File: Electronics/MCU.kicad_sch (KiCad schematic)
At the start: 6 parts

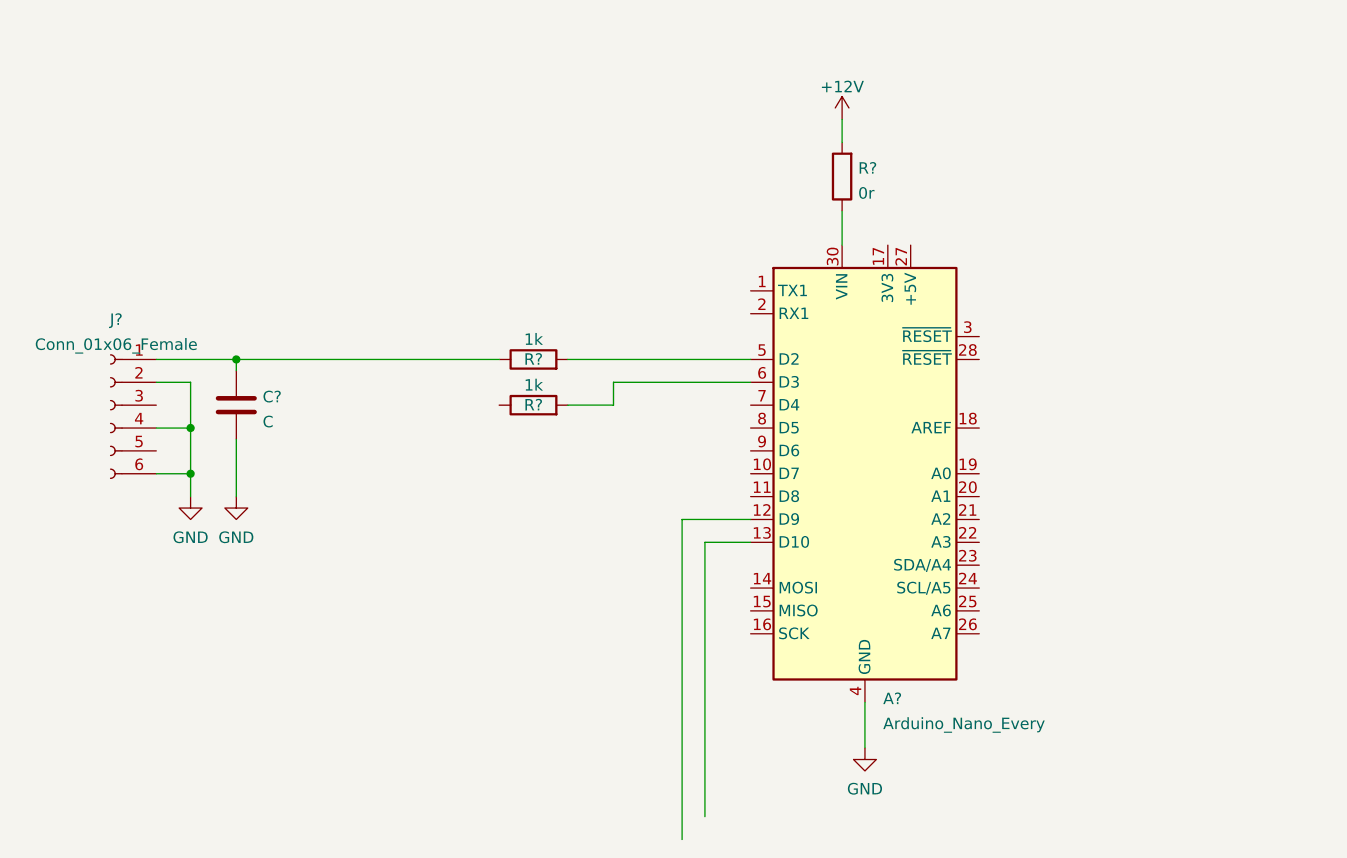
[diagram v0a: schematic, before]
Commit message: Added third half bridge for BLDC applications
Signed-off-by: Finder <aki.kuusela@findersee.fi>
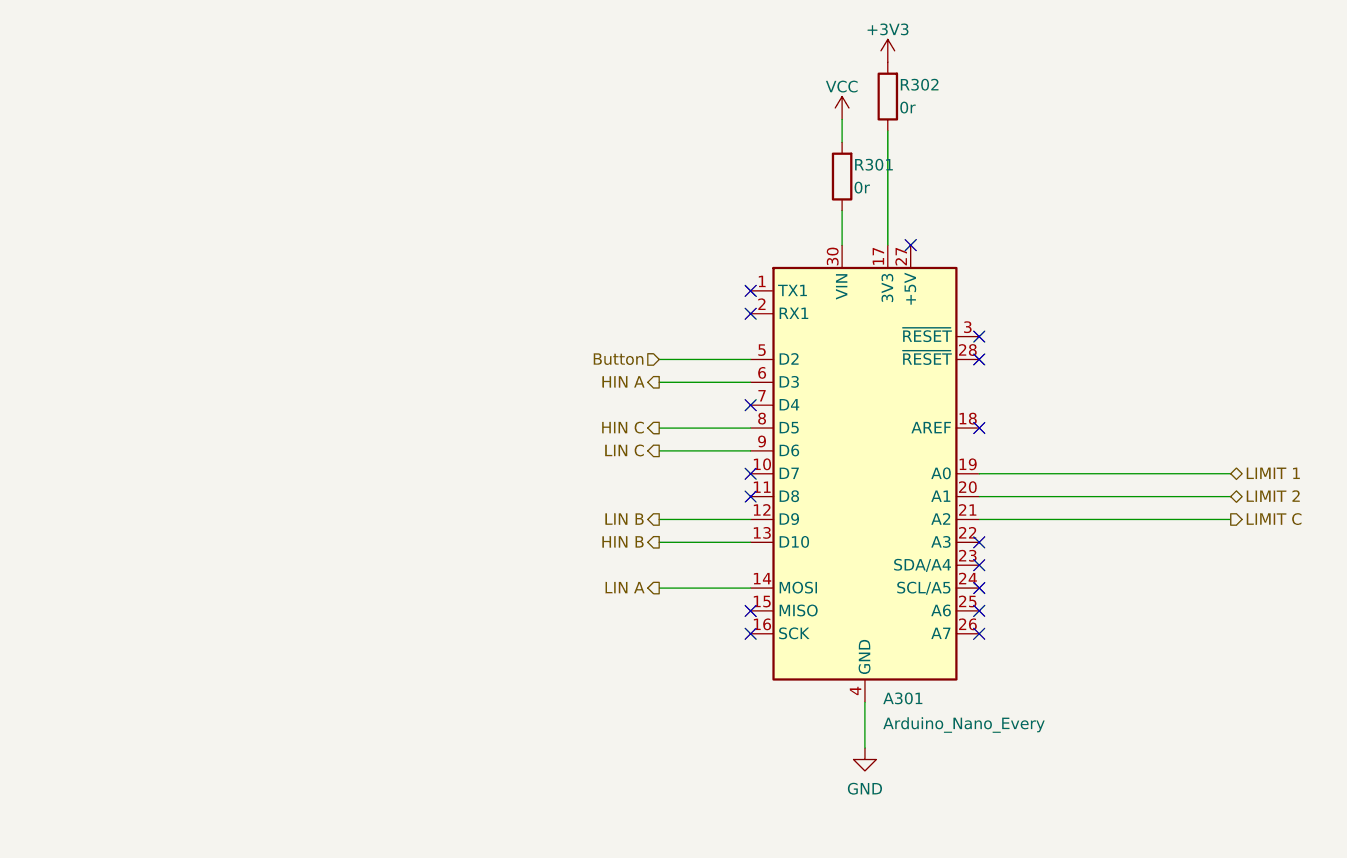
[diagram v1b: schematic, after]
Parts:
- removed C?: C, symbol Device:C
- removed J?: Conn_01x06_Female, TerminalBlock:TerminalBlock_bornier-6_P5.08mm, symbol Connector:Conn_01x06_Female
- removed R? (x2): 1k, digikey-footprints:0603, symbol Device:R
- added R302: 0r, digikey-footprints:0805, symbol Device:R
- gave numbers to parts that had none: 2
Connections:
- net HIN A: now reaches A301.6 (D3)
- net Button: now reaches A301.5 (D2)
- net LIN B: now reaches A301.12 (D9)
- net HIN B: now reaches A301.13 (D10)
- net LIN A: now reaches A301.14 (MOSI)
- net at A301.17 (3V3): now also R302.1
- net LIMIT 1: now reaches A301.19 (A0)
- net LIMIT 2: now reaches A301.20 (A1)
- net LIMIT C: now reaches A301.21 (A2)
- net HIN C: now reaches A301.8 (D5)
- net LIN C: now reaches A301.9 (D6)
- net +12V renamed VCC
- new net +3V3: R302.2
- no-connect marks 0 -> 16

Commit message: Layout update
Signed-off-by: Aki Kuusela <git@findersee.fi>
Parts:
- added C301: 100n, Capacitor_SMD:C_0603_1608Metric_Pad1.08x0.95mm_HandSolder, symbol Device:C
- added U301: 74HC86, Package_SO:SO-14_3.9x8.65mm_P1.27mm, symbol 74xx:74HC86
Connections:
- net +3V3: now also C301.2, U301.14 (VCC)
- net Button: now also U301.6
- net GND: now also C301.1, U301.10, U301.12, U301.13, U301.7 (GND), U301.9
- new net: U301.3, U301.4
- new net HALL A: U301.1
- new net HALL B: U301.2
- new net HALL C: U301.5
- no-connect marks 16 -> 18

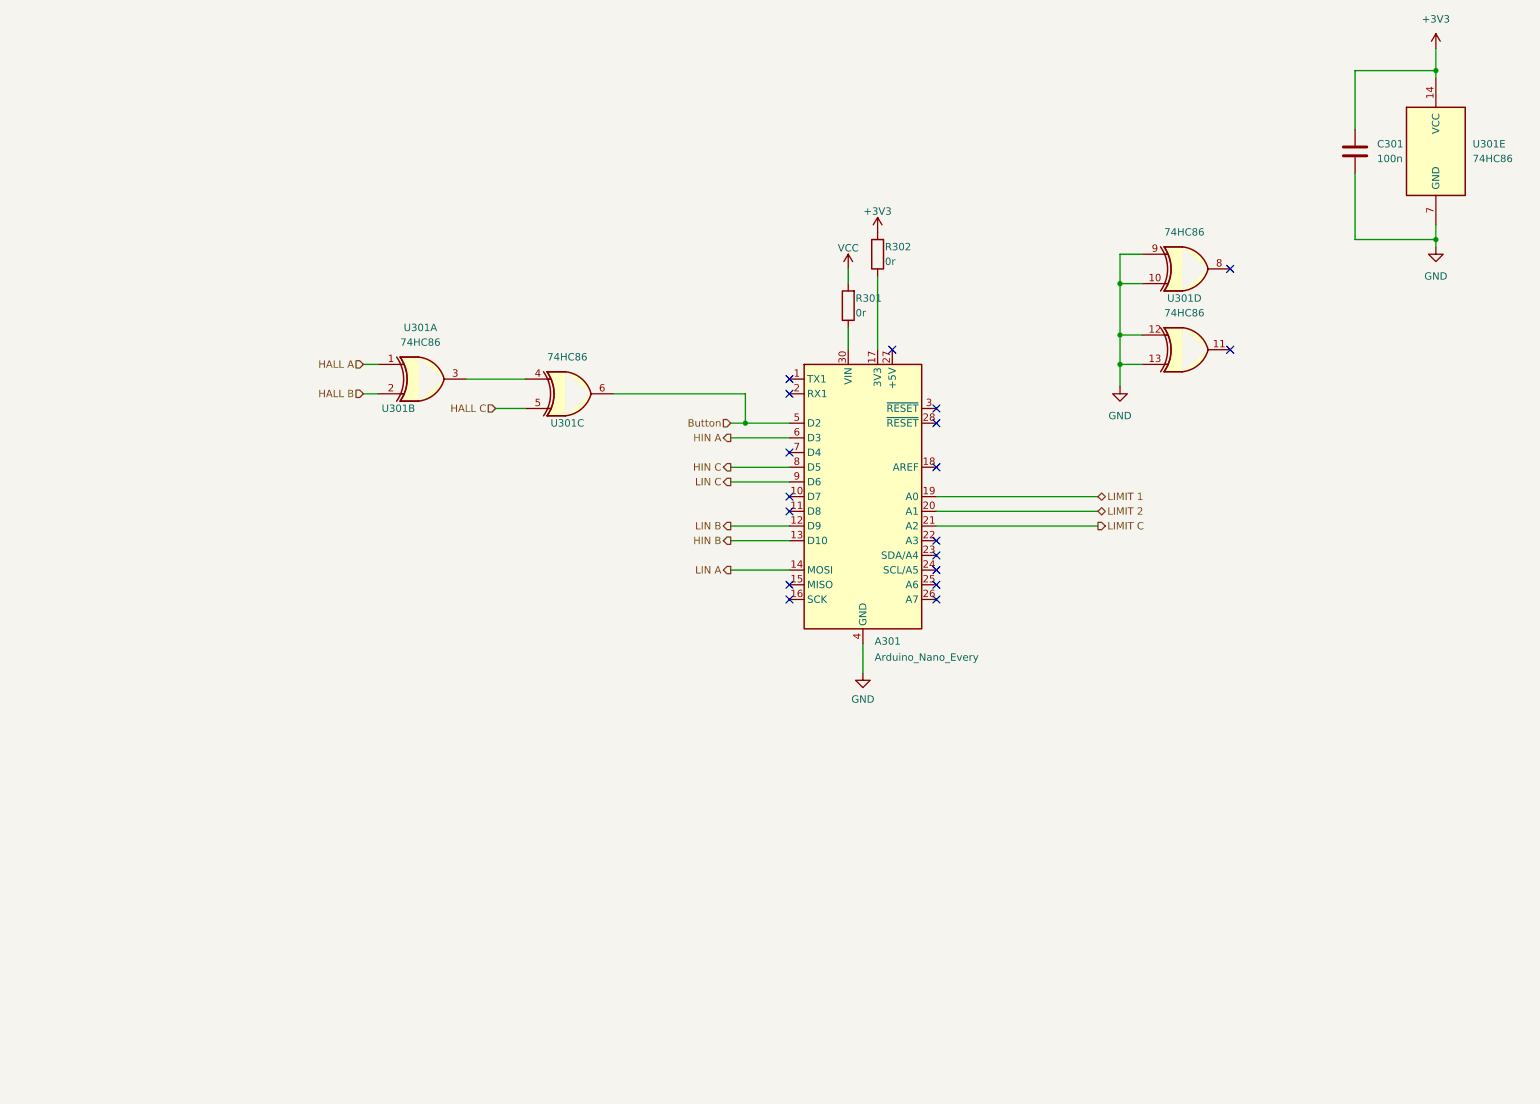
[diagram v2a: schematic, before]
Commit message: Added hall sensor circuitry
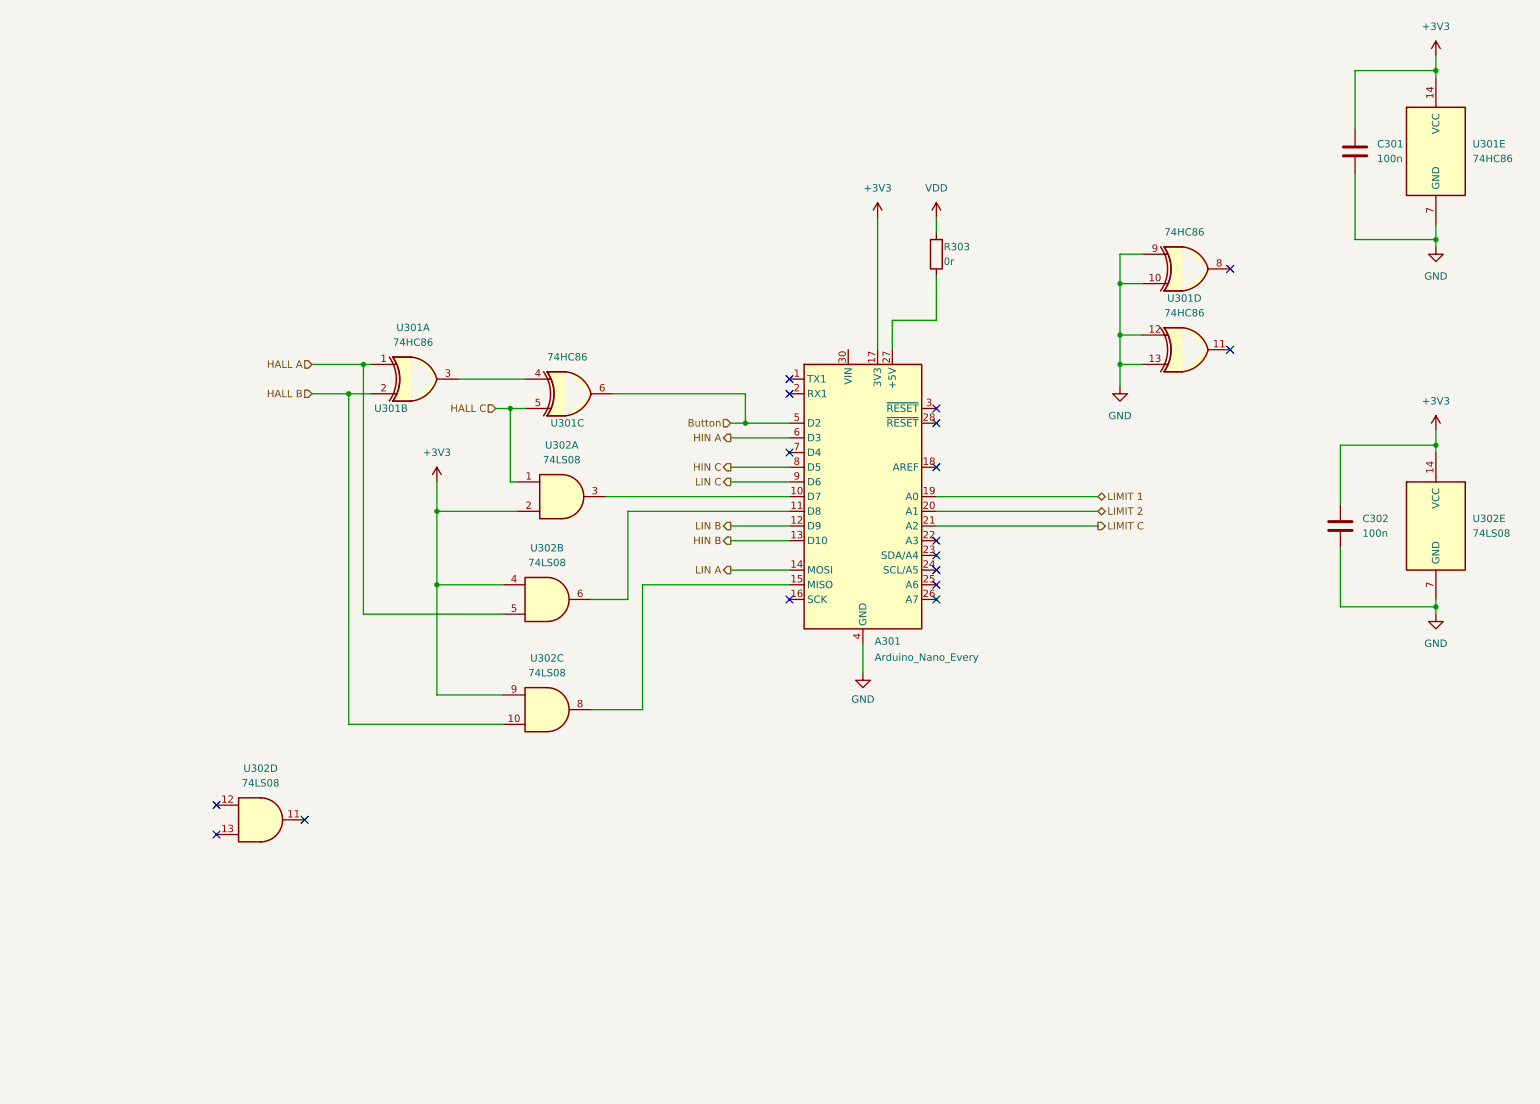
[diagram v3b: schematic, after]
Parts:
- removed R301, R302: 0r, digikey-footprints:0805, symbol Device:R
- added C302: 100n, Capacitor_SMD:C_0603_1608Metric_Pad1.08x0.95mm_HandSolder, symbol Device:C
- added R303: 0r, digikey-footprints:0805, symbol Device:R
- added U302: 74LS08, symbol 74xx:74LS08
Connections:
- net +3V3: now also A301.17 (3V3), C302.2, U302.14 (VCC), U302.2, U302.4, U302.9
- net GND: now also C302.1, U302.7 (GND)
- net HALL A: now also U302.5
- net HALL B: now also U302.10
- net HALL C: now also U302.1
- net at A301.10 (D7): now also U302.3
- net at A301.11 (D8): now also U302.6
- net at A301.15 (MISO): now also U302.8
- net at A301.27 (+5V): now also R303.1
- new net VDD: R303.2
- no-connect marks 18 -> 17
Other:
- moved on the sheet: U301A

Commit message: Added Current sensor finalized layout version 0.1
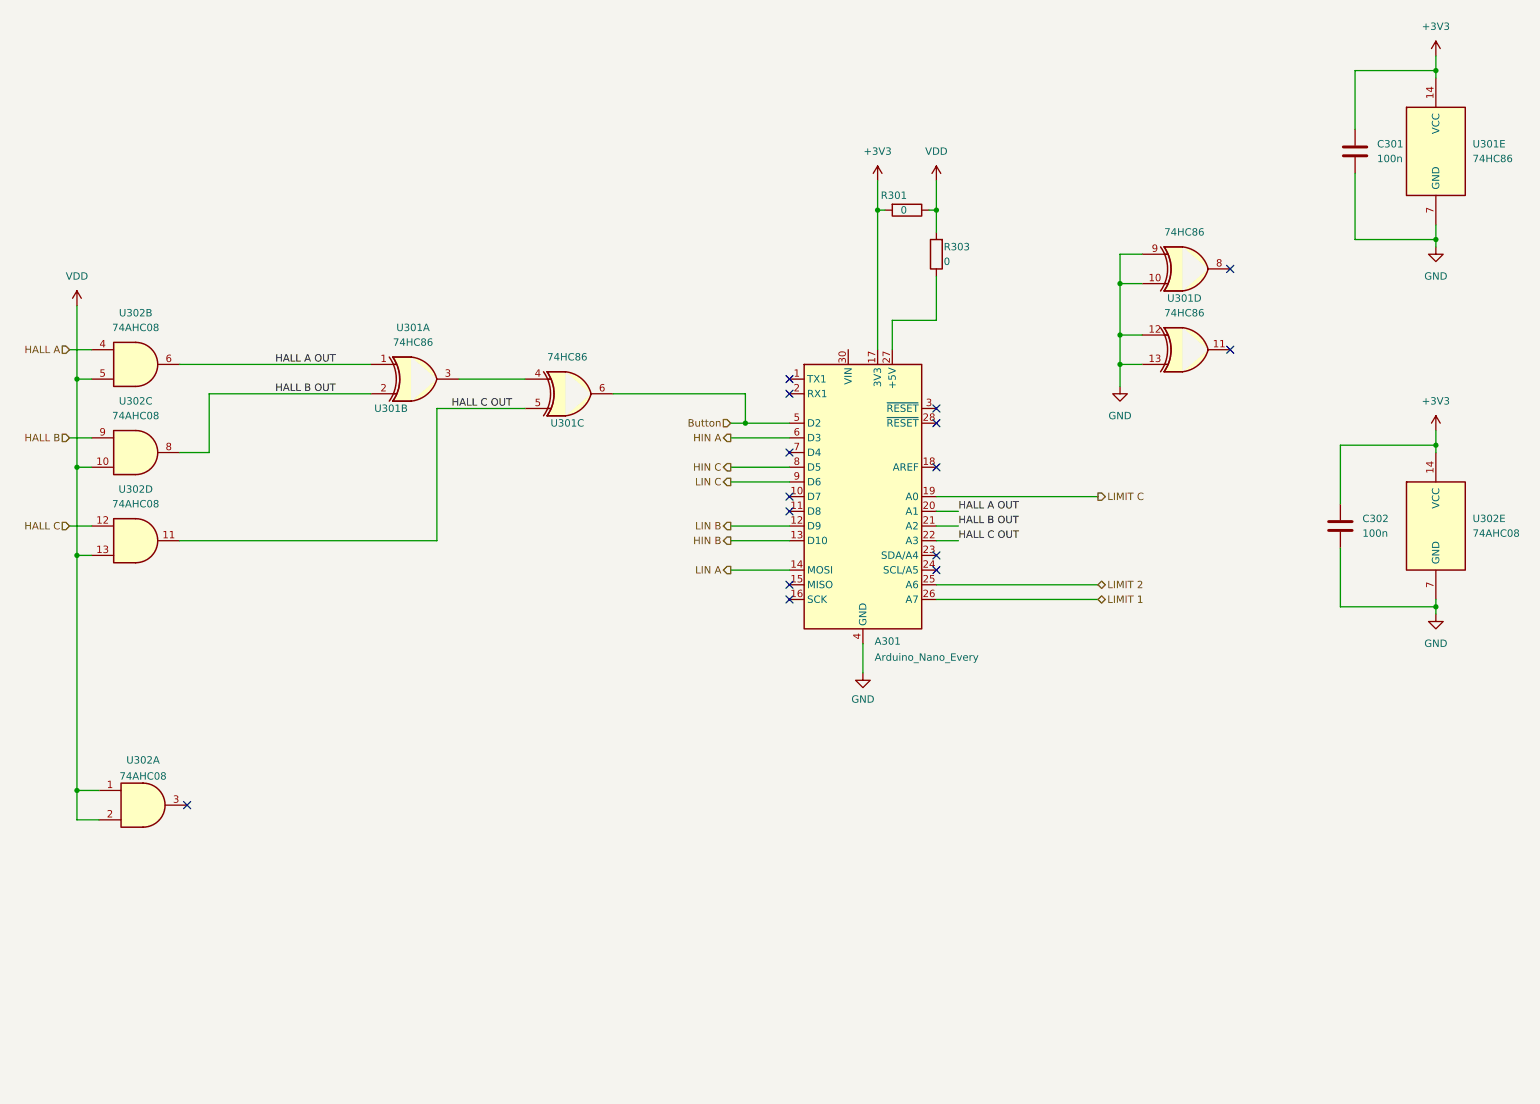
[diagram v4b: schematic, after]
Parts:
- added R301: 0, Resistor_SMD:R_0603_1608Metric_Pad0.98x0.95mm_HandSolder, symbol Device:R
- R303: value 0r -> 0; footprint digikey-footprints:0805 -> Resistor_SMD:R_0603_1608Metric_Pad0.98x0.95mm_HandSolder
- U302: value 74LS08 -> 74AHC08; footprint (none) -> Package_SO:SO-14_3.9x8.65mm_P1.27mm
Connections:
- net +3V3: now also R301.2; no longer U302.2, U302.4, U302.9
- net HALL A: now also U302.4; no longer U301.1, U302.5
- net HALL B: now also U302.9; no longer U301.2, U302.10
- net HALL C: now also U302.12; no longer U301.5, U302.1
- net LIMIT 1: now also A301.26 (A7); no longer A301.19 (A0)
- net LIMIT 2: now also A301.25 (A6); no longer A301.20 (A1)
- net LIMIT C: now also A301.19 (A0); no longer A301.21 (A2)
- net VDD: now also U302.1, U302.10, U302.13, U302.2, U302.5, R301.1
- net at A301.15 (MISO): no longer U302.8
- net at A301.10 (D7): no longer U302.3
- net at A301.11 (D8): no longer U302.6
- net HALL C OUT: now reaches A301.22 (A3)
- net HALL C OUT: now also U301.5, U302.11
- new net HALL A OUT: A301.20 (A1), U301.1, U302.6
- new net HALL B OUT: A301.21 (A2), U301.2, U302.8
- no-connect marks 17 -> 15
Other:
- moved on the sheet: U302A, U302B, U302C, U302D
